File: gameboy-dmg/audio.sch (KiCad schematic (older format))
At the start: 19 parts, among them J1 Conn_01x02, U6 PAM8302AAS

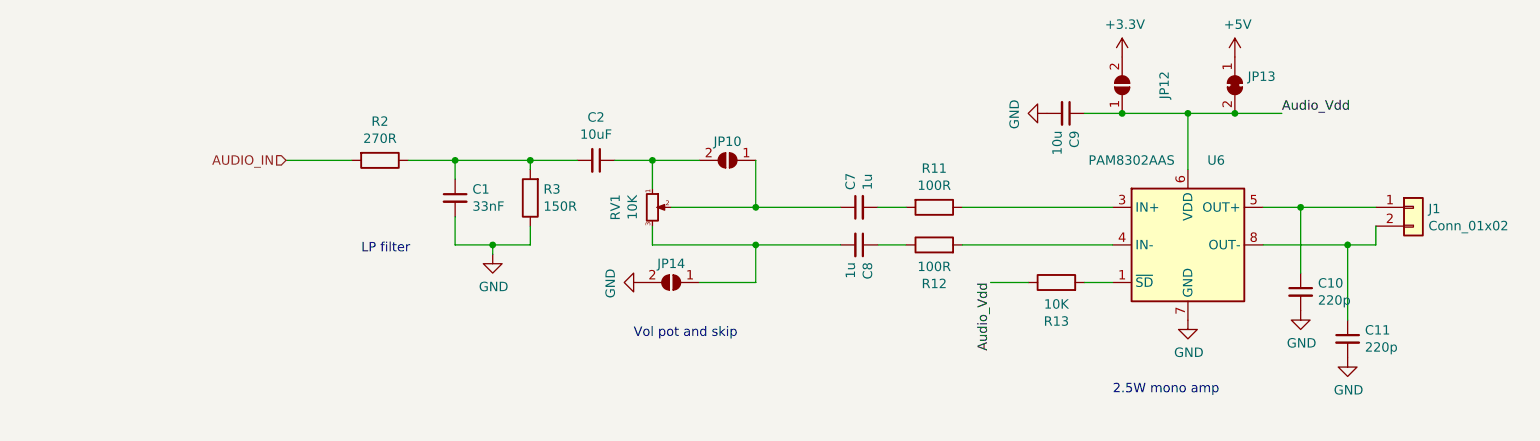
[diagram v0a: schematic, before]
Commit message: Added unroputed and unchecked horizontal vol pot
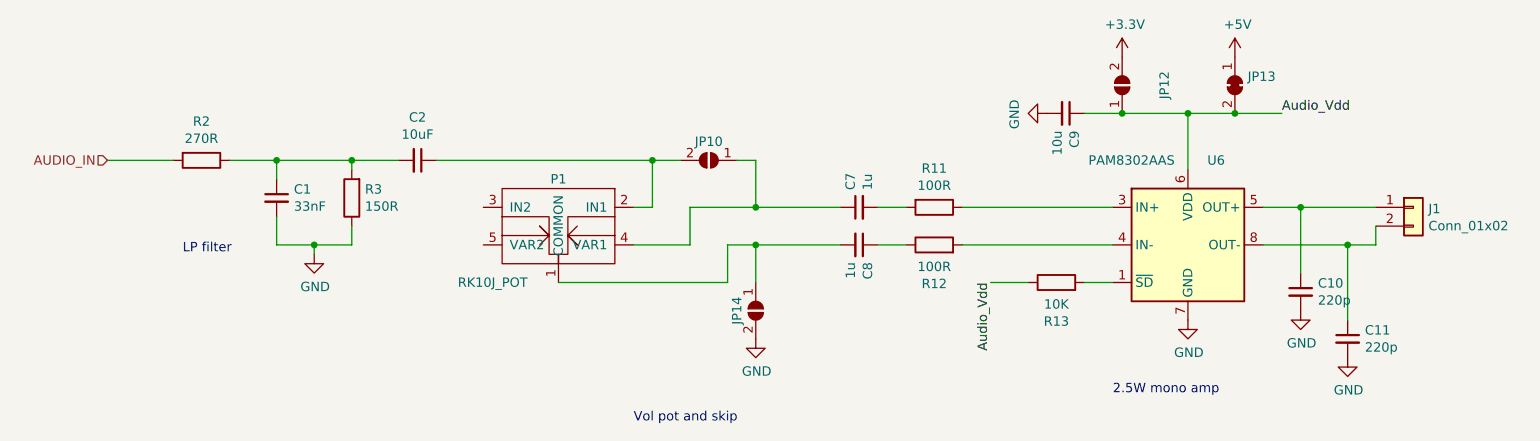
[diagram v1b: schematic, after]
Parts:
- removed RV1: 10K, symbol Device:R_POT_Small
- added P1: RK10J_POT, pad:R503_POT, symbol gameboy_power:RK10J_POT
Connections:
- net at C2.1, JP10.2 (B): now also P1.2 (IN1)
- net at C8.2, JP14.1 (A): now also P1.1 (COMMON)
- net at C7.1, JP10.1 (A): now also P1.4 (VAR1)
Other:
- moved on the sheet: C1, C2, JP10, JP14, R2, R3
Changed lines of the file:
@@
 L Device:R R2
 U 1 1 5E819B2F
-P 4500 4000
-F 0 "R2" V 4293 4000 50  0000 C CNN
-F 1 "270R" V 4384 4000 50  0000 C CNN
-F 2 "Resistor_SMD:R_0603_1608Metric" V 4430 4000 50  0001 C CNN
-F 3 "~" H 4500 4000 50  0001 C CNN
-	1    4500 4000
+P 3550 4000
+F 0 "R2" V 3343 4000 50  0000 C CNN
+F 1 "270R" V 3434 4000 50  0000 C CNN
+F 2 "Resistor_SMD:R_0603_1608Metric" V 3480 4000 50  0001 C CNN
+F 3 "~" H 3550 4000 50  0001 C CNN
+	1    3550 4000
 	0    1    1    0
 $EndComp
@@
 L Device:R R3
 U 1 1 5E819B35
-P 5300 4200
-F 0 "R3" H 5230 4154 50  0000 R CNN
-F 1 "150R" H 5230 4245 50  0000 R CNN
-F 2 "Resistor_SMD:R_0603_1608Metric" V 5230 4200 50  0001 C CNN
-F 3 "~" H 5300 4200 50  0001 C CNN
-	1    5300 4200
+P 4350 4200
+F 0 "R3" H 4280 4154 50  0000 R CNN
+F 1 "150R" H 4280 4245 50  0000 R CNN
+F 2 "Resistor_SMD:R_0603_1608Metric" V 4280 4200 50  0001 C CNN
+F 3 "~" H 4350 4200 50  0001 C CNN
+	1    4350 4200
 	-1   0    0    1
 $EndComp
@@
 L Device:C_Small C1
 U 1 1 5E819B3B
-P 4900 4200
-F 0 "C1" H 4992 4246 50  0000 L CNN
-F 1 "33nF" H 4992 4155 50  0000 L CNN
-F 2 "Capacitor_SMD:C_0603_1608Metric" H 4900 4200 50  0001 C CNN
-F 3 "~" H 4900 4200 50  0001 C CNN
-	1    4900 4200
+P 3950 4200
+F 0 "C1" H 4042 4246 50  0000 L CNN
+F 1 "33nF" H 4042 4155 50  0000 L CNN
+F 2 "Capacitor_SMD:C_0603_1608Metric" H 3950 4200 50  0001 C CNN
+F 3 "~" H 3950 4200 50  0001 C CNN
+	1    3950 4200
 	1    0    0    -1
 $EndComp
@@
 L Device:C_Small C2
 U 1 1 5E819B41
-P 5650 4000
-F 0 "C2" V 5421 4000 50  0000 C CNN
-F 1 "10uF" V 5512 4000 50  0000 C CNN
-F 2 "Capacitor_THT:CP_Radial_D5.0mm_P2.00mm" H 5650 4000 50  0001 C CNN
-F 3 "~" H 5650 4000 50  0001 C CNN
-	1    5650 4000
-	0    1    1    0
-$EndComp
-Wire Wire Line
-	5550 4000 5300 4000
-Wire Wire Line
-	4900 4100 4900 4000
-Connection ~ 4900 4000
-Wire Wire Line
-	4900 4000 4650 4000
-Wire Wire Line
-	5300 4050 5300 4000
-Connection ~ 5300 4000
-Wire Wire Line
-	5300 4000 4900 4000
-Wire Wire Line
-	4900 4300 4900 4450
-Wire Wire Line
-	4900 4450 5100 4450
-Wire Wire Line
-	5300 4450 5300 4350
+P 4700 4000
+F 0 "C2" V 4471 4000 50  0000 C CNN
+F 1 "10uF" V 4562 4000 50  0000 C CNN
+F 2 "Capacitor_THT:CP_Radial_D5.0mm_P2.00mm" H 4700 4000 50  0001 C CNN
+F 3 "~" H 4700 4000 50  0001 C CNN
+	1    4700 4000
+	0    1    1    0
+$EndComp
+Wire Wire Line
+	4600 4000 4350 4000
+Wire Wire Line
+	3950 4100 3950 4000
+Connection ~ 3950 4000
+Wire Wire Line
+	3950 4000 3700 4000
+Wire Wire Line
+	4350 4050 4350 4000
+Connection ~ 4350 4000
+Wire Wire Line
+	4350 4000 3950 4000
+Wire Wire Line
+	3950 4300 3950 4450
+Wire Wire Line
+	3950 4450 4150 4450
+Wire Wire Line
+	4350 4450 4350 4350
 $Comp
 L power:GND #PWR0103
 U 1 1 5E819B51
-P 5100 4500
-F 0 "#PWR0103" H 5100 4250 50  0001 C CNN
-F 1 "GND" H 5105 4327 50  0000 C CNN
-F 2 "" H 5100 4500 50  0001 C CNN
-F 3 "" H 5100 4500 50  0001 C CNN
-	1    5100 4500
-	1    0    0    -1
-$EndComp
-Wire Wire Line
-	5100 4500 5100 4450
-Connection ~ 5100 4450
-Wire Wire Line
-	5100 4450 5300 4450
-Wire Wire Line
-	4000 4000 4350 4000
+P 4150 4500
+F 0 "#PWR0103" H 4150 4250 50  0001 C CNN
+F 1 "GND" H 4155 4327 50  0000 C CNN
+F 2 "" H 4150 4500 50  0001 C CNN
+F 3 "" H 4150 4500 50  0001 C CNN
+	1    4150 4500
+	1    0    0    -1
+$EndComp
+Wire Wire Line
+	4150 4500 4150 4450
+Connection ~ 4150 4450
+Wire Wire Line
+	4150 4450 4350 4450
+Wire Wire Line
+	3050 4000 3400 4000
 $Comp
 L Connector_Generic:Conn_01x02 J1
@@
 	1    0    0    -1
 $EndComp
-Text HLabel 4000 4000 0    50   Input ~ 0
+Text HLabel 3050 4000 0    50   Input ~ 0
 AUDIO_IN
 $Comp
 L Jumper:SolderJumper_2_Open JP10
 U 1 1 5E9290A5
-P 6350 4000
-F 0 "JP10" H 6350 3900 50  0000 C CNN
-F 1 "SolderJumper_2_Open" H 6350 3866 50  0001 C CNN
-F 2 "Jumper:SolderJumper-2_P1.3mm_Open_RoundedPad1.0x1.5mm" H 6350 4000 50  0001 C CNN
-F 3 "~" H 6350 4000 50  0001 C CNN
-	1    6350 4000
+P 6250 4000
+F 0 "JP10" H 6250 3900 50  0000 C CNN
+F 1 "SolderJumper_2_Open" H 6250 3866 50  0001 C CNN
+F 2 "Jumper:SolderJumper-2_P1.3mm_Open_RoundedPad1.0x1.5mm" H 6250 4000 50  0001 C CNN
+F 3 "~" H 6250 4000 50  0001 C CNN
+	1    6250 4000
 	-1   0    0    1
 $EndComp
@@
 $EndComp
 $Comp
-L Device:R_POT_Small RV1
-U 1 1 5E925F2A
-P 5950 4250
-F 0 "RV1" V 5753 4250 50  0000 C CNN
-F 1 "10K" V 5844 4250 50  0000 C CNN
-F 2 "" H 5950 4250 50  0001 C CNN
-F 3 "~" H 5950 4250 50  0001 C CNN
-	1    5950 4250
-	1    0    0    -1
-$EndComp
-$Comp
 L Jumper:SolderJumper_2_Open JP14
 U 1 1 5E836F0B
-P 6050 4650
-F 0 "JP14" H 6050 4550 50  0000 C CNN
-F 1 "SolderJumper_2_Open" H 6050 4516 50  0001 C CNN
-F 2 "Jumper:SolderJumper-2_P1.3mm_Open_RoundedPad1.0x1.5mm" H 6050 4650 50  0001 C CNN
-F 3 "~" H 6050 4650 50  0001 C CNN
-	1    6050 4650
-	-1   0    0    1
+P 6500 4800
+F 0 "JP14" H 6500 4700 50  0000 C CNN
+F 1 "SolderJumper_2_Open" H 6500 4666 50  0001 C CNN
+F 2 "Jumper:SolderJumper-2_P1.3mm_Open_RoundedPad1.0x1.5mm" H 6500 4800 50  0001 C CNN
+F 3 "~" H 6500 4800 50  0001 C CNN
+	1    6500 4800
+	0    1    1    0
 $EndComp
 $Comp
 L power:GND #PWR0104
 U 1 1 5E838D4A
-P 5900 4650
-F 0 "#PWR0104" H 5900 4400 50  0001 C CNN
-F 1 "GND" H 5905 4477 50  0000 C CNN
-F 2 "" H 5900 4650 50  0001 C CNN
-F 3 "" H 5900 4650 50  0001 C CNN
-	1    5900 4650
-	0    1    1    0
-$EndComp
-Wire Wire Line
-	5750 4000 5950 4000
-Wire Wire Line
-	5950 4000 5950 4150
-Wire Wire Line
-	6050 4250 6500 4250
-Wire Wire Line
-	5950 4350 5950 4450
-Wire Wire Line
-	5950 4450 6500 4450
-Wire Wire Line
-	5950 4000 6200 4000
+P 6500 4950
+F 0 "#PWR0104" H 6500 4700 50  0001 C CNN
+F 1 "GND" H 6505 4777 50  0000 C CNN
+F 2 "" H 6500 4950 50  0001 C CNN
+F 3 "" H 6500 4950 50  0001 C CNN
+	1    6500 4950
+	1    0    0    -1
+$EndComp
+Wire Wire Line
+	5950 4000 6100 4000
 Connection ~ 5950 4000
 Wire Wire Line
 	6500 4000 6500 4250
-Connection ~ 6500 4250
 Wire Wire Line
 	6500 4250 6950 4250
 Wire Wire Line
 	6500 4650 6500 4450
-Connection ~ 6500 4450
 Wire Wire Line
 	6500 4450 6950 4450
-Text Notes 5850 4950 0    50   ~ 0
+Text Notes 5850 5400 0    50   ~ 0
 Vol pot and skip
-Text Notes 4400 4500 0    50   ~ 0
+Text Notes 3450 4500 0    50   ~ 0
 LP filter
 Text Notes 8400 5250 0    50   ~ 0
 2.5W mono amp
-Wire Wire Line
-	6200 4650 6500 4650
+$Comp
+L gameboy_power:RK10J_POT P1
+U 1 1 5E85AA44
+P 5500 4200
+F 0 "P1" H 5550 4300 50  0000 C CNN
+F 1 "RK10J_POT" H 5900 3750 50  0000 C CNN
+F 2 "pad:R503_POT" H 5500 4200 50  0001 C CNN
+F 3 "" H 5500 4200 50  0001 C CNN
+	1    5500 4200
+	-1   0    0    -1
+$EndComp
+Wire Wire Line
+	5850 4250 5950 4250
+Wire Wire Line
+	5950 4000 5950 4250
+Wire Wire Line
+	5850 4450 6150 4450
+Wire Wire Line
+	6150 4450 6150 4250
+Wire Wire Line
+	6150 4250 6500 4250
+Connection ~ 6500 4250
+Wire Wire Line
+	5450 4650 6350 4650
+Wire Wire Line
+	6350 4650 6350 4450
+Wire Wire Line
+	6350 4450 6500 4450
+Connection ~ 6500 4450
+Wire Wire Line
+	4800 4000 5950 4000
+Wire Wire Line
+	6500 4000 6400 4000
 $EndSCHEMATC
